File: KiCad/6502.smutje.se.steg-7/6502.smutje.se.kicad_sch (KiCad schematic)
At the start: 12 parts, among them U1 W65C02S, U2 LCD-016N002L, U3 W65C22, U4 74HC00

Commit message: Steg 6 & 7: KiCad-scheman uppdaterade, HTML-sidor fixade, main.cpp för VIA+LCD
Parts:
- removed R5: (no value), symbol Device:R_US
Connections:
- net Earth: now also U1.36 (BE)
- net at A1.D2 (D2_INT0), U3.24 (CS1), U3.25 (ϕ2): now also U1.37 (ϕ0); no longer U1.39 (ϕ2)

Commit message: Uppdatera steg-6 och steg-7 PNG:er med BE→+5V
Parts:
- added R5: (no value), symbol Device:R_US
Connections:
- net +5V: now also R5.1
- net Earth: no longer U1.36 (BE)
- new net: R5.2, U1.36 (BE)
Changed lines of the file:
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@@
 		)
 	)
-	(wire
-		(pts
-			(xy 80.01 66.04) (xy 80.01 68.58)
-		)
-		(stroke
-			(width 0)
-			(type default)
-		)
-	)
 	(bus
 		(pts
@@
 	(wire
 		(pts
+			(xy 62.23 66.04) (xy 85.09 66.04)
+		)
+		(stroke
+			(width 0)
+			(type default)
+		)
+	)
+	(wire
+		(pts
 			(xy 222.25 87.63) (xy 236.22 87.63)
 		)
@@
 	(wire
 		(pts
-			(xy 222.25 82.55) (xy 236.22 82.55)
+			(xy 62.23 63.5) (xy 62.23 66.04)
 		)
 		(stroke
@@
 	(wire
 		(pts
-			(xy 194.31 88.9) (xy 203.2 88.9)
+			(xy 222.25 82.55) (xy 236.22 82.55)
 		)
 		(stroke
@@
 	(wire
 		(pts
-			(xy 105.41 73.66) (xy 116.84 73.66)
+			(xy 194.31 88.9) (xy 203.2 88.9)
 		)
 		(stroke
@@
 	(wire
 		(pts
-			(xy 233.68 146.05) (xy 233.68 148.59)
+			(xy 105.41 73.66) (xy 116.84 73.66)
 		)
 		(stroke
@@
 	(wire
 		(pts
-			(xy 302.26 85.09) (xy 309.88 85.09)
+			(xy 233.68 146.05) (xy 233.68 148.59)
 		)
 		(stroke
@@
 	(wire
 		(pts
-			(xy 85.09 66.04) (xy 80.01 66.04)
+			(xy 302.26 85.09) (xy 309.88 85.09)
 		)
 		(stroke
@@
 	)
 	(symbol
+		(lib_id "Device:R_US")
+		(at 62.23 59.69 0)
+		(unit 1)
+		(body_style 1)
+		(exclude_from_sim no)
+		(in_bom yes)
+		(on_board yes)
+		(in_pos_files yes)
+		(dnp no)
+		(property "Reference" "R5"
+			(at 64.77 58.4199 90)
+			(show_name no)
+			(do_not_autoplace no)
+			(effects
+				(font
+					(size 1.27 1.27)
+				)
+				(justify left)
+			)
+		)
+		(property "Value" ""
+			(at 64.77 60.9599 0)
+			(show_name no)
+			(do_not_autoplace no)
+			(effects
+				(font
+					(size 1.27 1.27)
+				)
+				(justify left)
+			)
+		)
+		(property "Footprint" ""
+			(at 63.246 59.944 90)
+			(hide yes)
+			(show_name no)
+			(do_not_autoplace no)
+			(effects
+				(font
+					(size 1.27 1.27)
+				)
+			)
+		)
+		(property "Datasheet" ""
+			(at 62.23 59.69 0)
+			(hide yes)
+			(show_name no)
+			(do_not_autoplace no)
+			(effects
+				(font
+					(size 1.27 1.27)
+				)
+			)
+		)
+		(property "Description" "Resistor, US symbol"
+			(at 62.23 59.69 0)
+			(hide yes)
+			(show_name no)
+			(do_not_autoplace no)
+			(effects
+				(font
+					(size 1.27 1.27)
+				)
+			)
+		)
+		(pin "1"
+		)
+		(pin "2"
+		)
+		(instances
+			(project "6502.smutje.se"
+				(path "/6aa7970e-7944-4a13-90e7-04df56da4812"
+					(reference "R5")
+					(unit 1)
+				)
+			)
+		)
+	)
+	(symbol
 		(lib_id "74xx:74HC00")
 		(at 142.24 31.75 0)
@@
 	(symbol
 		(lib_id "power:+5V")
+		(at 62.23 55.88 0)
+		(unit 1)
+		(body_style 1)
+		(exclude_from_sim no)
+		(in_bom yes)
+		(on_board yes)
+		(in_pos_files yes)
+		(dnp no)
+		(fields_autoplaced yes)
+		(property "Reference" "#PWR09"
+			(at 62.23 59.69 0)
+			(hide yes)
+			(show_name no)
+			(do_not_autoplace no)
+			(effects
+				(font
+					(size 1.27 1.27)
+				)
+			)
+		)
+		(property "Value" "+5V"
+			(at 62.23 50.8 0)
+			(show_name no)
+			(do_not_autoplace no)
+			(effects
+				(font
+					(size 1.27 1.27)
+				)
+			)
+		)
+		(property "Footprint" ""
+			(at 62.23 55.88 0)
+			(hide yes)
+			(show_name no)
+			(do_not_autoplace no)
+			(effects
+				(font
+					(size 1.27 1.27)
+				)
+			)
+		)
+		(property "Datasheet" ""
+			(at 62.23 55.88 0)
+			(hide yes)
+			(show_name no)
+			(do_not_autoplace no)
+			(effects
+				(font
+					(size 1.27 1.27)
+				)
+			)
+		)
+		(property "Description" "Power symbol creates a global label with name \"+5V\""
+			(at 62.23 55.88 0)
+			(hide yes)
+			(show_name no)
+			(do_not_autoplace no)
+			(effects
+				(font
+					(size 1.27 1.27)
+				)
+			)
+		)
+		(pin "1"
+		)
+		(instances
+			(project "6502.smutje.se"
+				(path "/6aa7970e-7944-4a13-90e7-04df56da4812"
+					(reference "#PWR09")
+					(unit 1)
+				)
+			)
+		)
+	)
+	(symbol
+		(lib_id "power:+5V")
 		(at 184.15 123.19 0)
 		(unit 1)
@@
 					(unit 1)
 				)
-			)
-		)
-	)
-	(symbol
-		(lib_id "power:Earth")
-		(at 80.01 68.58 0)
-		(unit 1)
-		(body_style 1)
-		(exclude_from_sim no)
-		(in_bom yes)
-		(on_board yes)
-		(in_pos_files yes)
-		(dnp no)
-		(fields_autoplaced yes)
-		(property "Reference" "#PWR09"
-			(at 80.01 74.93 0)
-			(hide yes)
-			(show_name no)
-			(do_not_autoplace no)
-			(effects
-				(font
-					(size 1.27 1.27)
-				)
-			)
-		)
-		(property "Value" "Earth"
-			(at 80.01 73.66 0)
-			(hide yes)
-			(show_name no)
-			(do_not_autoplace no)
-			(effects
-				(font
-					(size 1.27 1.27)
-				)
-			)
-		)
-		(property "Footprint" ""
-			(at 80.01 68.58 0)
-			(hide yes)
-			(show_name no)
-			(do_not_autoplace no)
-			(effects
-				(font
-					(size 1.27 1.27)
-				)
-			)
-		)
-		(property "Datasheet" ""
-			(at 80.01 68.58 0)
-			(hide yes)
-			(show_name no)
-			(do_not_autoplace no)
-			(effects
-				(font
-					(size 1.27 1.27)
-				)
-			)
-		)
-		(property "Description" "Power symbol creates a global label with name \"Earth\""
-			(at 80.01 68.58 0)
-			(hide yes)
-			(show_name no)
-			(do_not_autoplace no)
-			(effects
-				(font
-					(size 1.27 1.27)
-				)
-			)
-		)
-		(pin "1"
-		)
-		(instances
-			(project "6502.smutje.se"
-				(path "/6aa7970e-7944-4a13-90e7-04df56da4812"
-					(reference "#PWR09")
-					(unit 1)
-				)

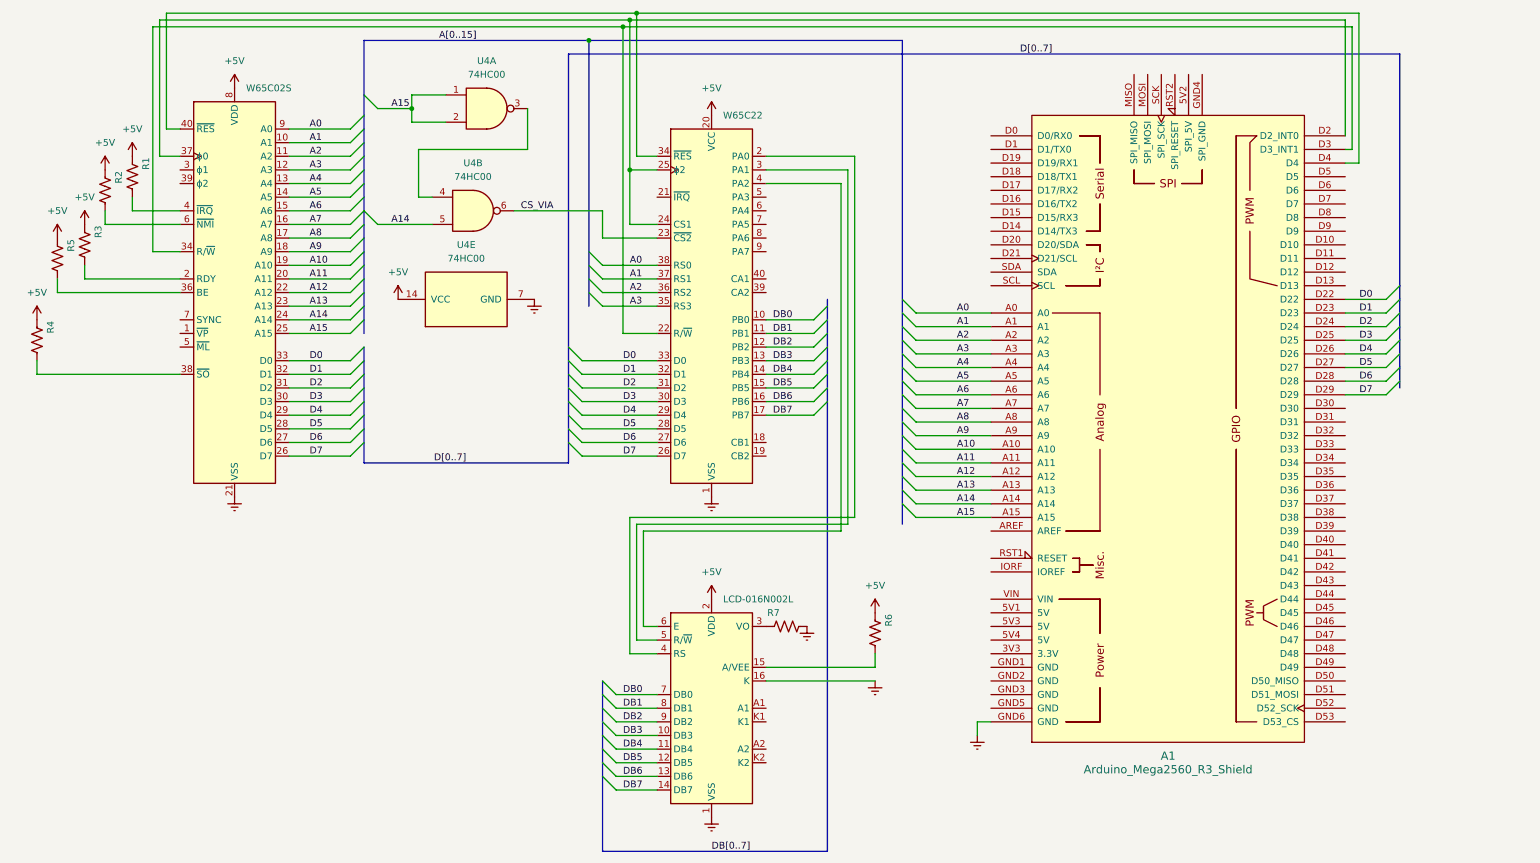
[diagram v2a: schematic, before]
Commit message: Steg 6 & 7: knappar + SYNC tillagda, nya PNG:er
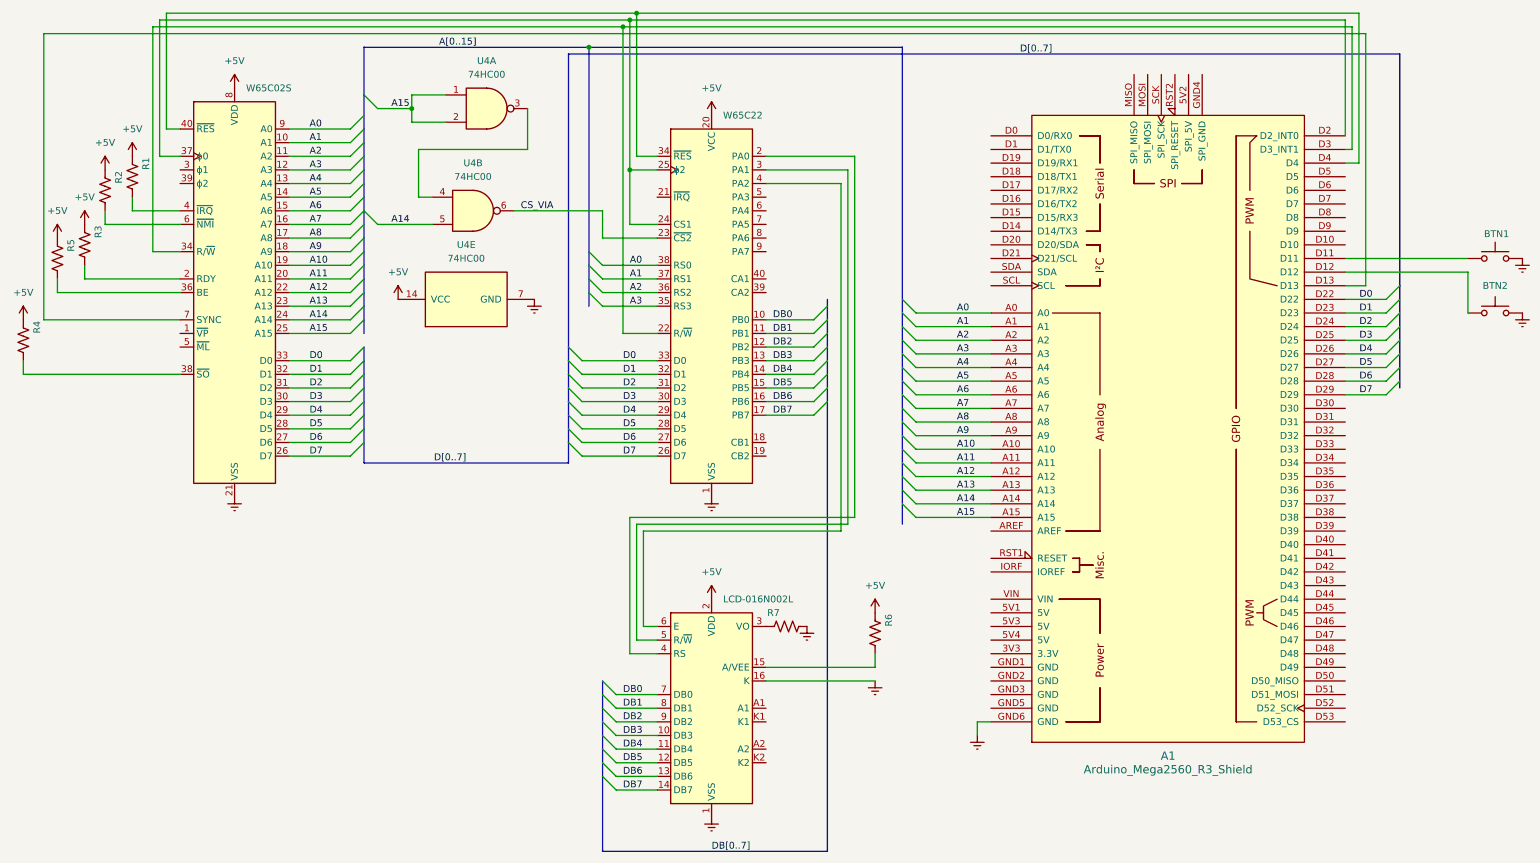
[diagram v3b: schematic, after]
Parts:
- added BTN1, BTN2: SW_Push, symbol Switch:SW_Push
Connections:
- net Earth: now also BTN1.2, BTN2.2
- net at A1.D11: now also BTN1.1
- net at A1.D12: now also BTN2.1
- net at A1.D13: now also U1.7 (SYNC)
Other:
- moved on the sheet: R4
